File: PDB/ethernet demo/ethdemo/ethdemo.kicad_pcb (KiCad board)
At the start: 4 copper layers, 77.5 x 67.5 mm, 99 parts, among them J1 0826-1X1T-GJ-F, J2 0826-1X1T-GJ-F, J3 Conn_01x05_Socket, Q1 CSD19538Q3AT, U1 STM32H742VGTx, U2 KSZ8863RLLI, U3 TPS23861PWR, Y1 25MHz

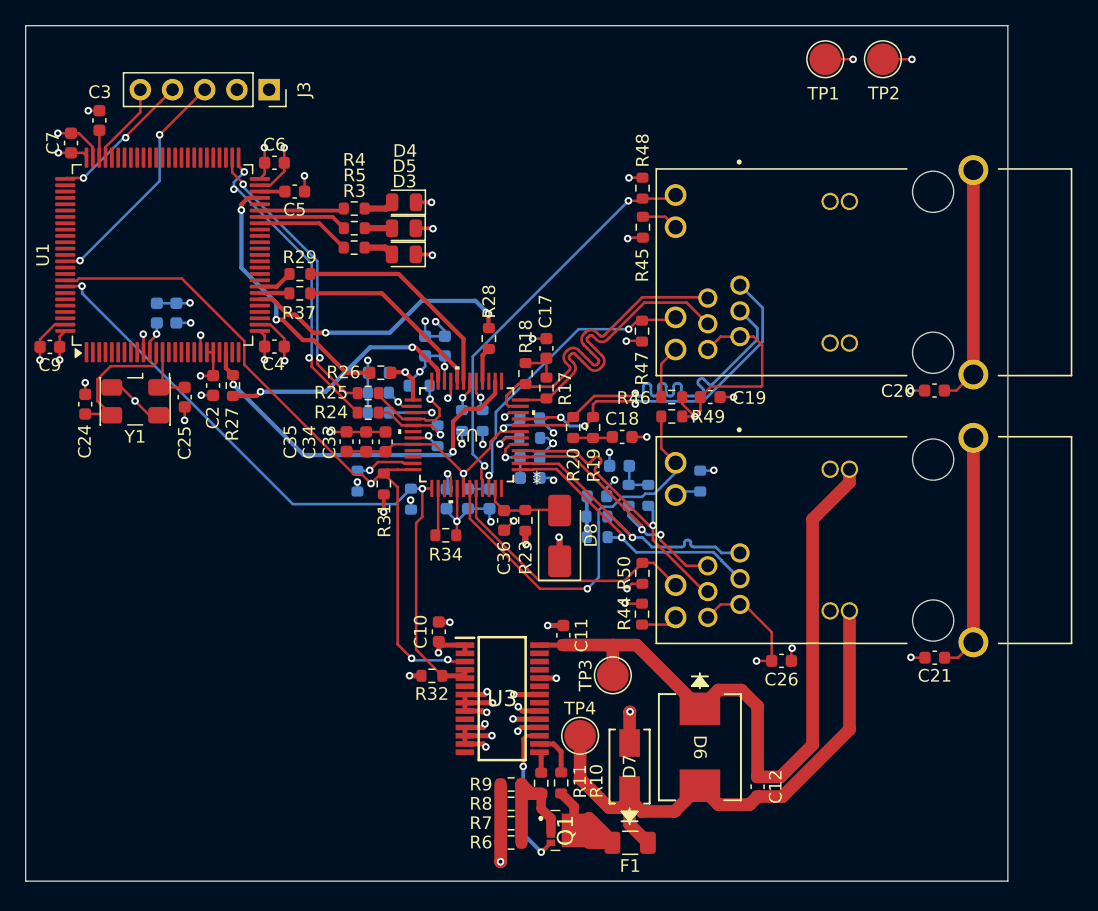
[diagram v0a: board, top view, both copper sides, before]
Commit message: routed usb and added power pads
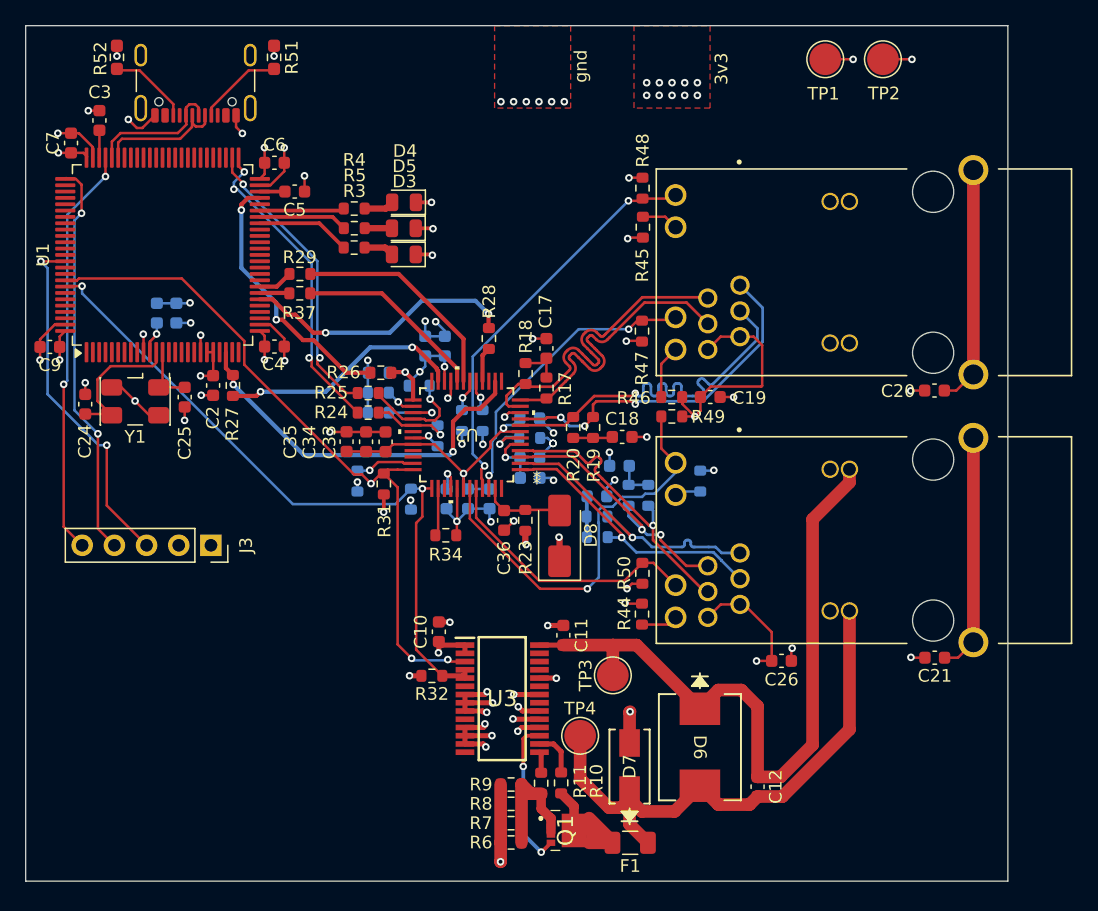
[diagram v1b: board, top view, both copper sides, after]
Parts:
- added J9: USB_C_Receptacle_USB2.0_16P, Connector_USB:USB_C_Receptacle_GCT_USB4105-xx-A_16P_TopMnt_Horizontal, F.Cu at (190.9, 40.9)
- added R51: 5.1k, Resistor_SMD:R_0603_1608Metric_Pad0.98x0.95mm_HandSolder, F.Cu at (197.1, 40.0)
- added R52: 5.1k, Resistor_SMD:R_0603_1608Metric_Pad0.98x0.95mm_HandSolder, F.Cu at (184.7, 40.0)
- moved J3 36.2 mm to (192.1, 78.5)
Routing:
- net /SWDIO: track 6.50 -> 32.6 mm, vias 0 -> 2
- net /SWCLK: track 11.4 -> 31.6 mm
- net /D-: track 0.00 -> 10.9 mm
- net /D+: track 0.00 -> 10.9 mm
- net /SWO/TRACE: track 18.7 -> 28.2 mm
- net Net-(J9-CC1): track 0.00 -> 6.82 mm
- net Net-(J9-CC2): track 0.00 -> 6.33 mm
- net GND: track 110.6 -> 116.7 mm, vias 55 -> 65
- net +3.3V: vias 28 -> 38
- added copper zone on F.Cu, net +3.3V
- added copper zone on F.Cu, net GND
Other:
- board text added: "3v3"
- board text added: "gnd"

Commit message: Satisfy DRC
I added poor for 48V and expanded GND for 2 power supply clips, ran DRC with JLC minimums and fixed problems
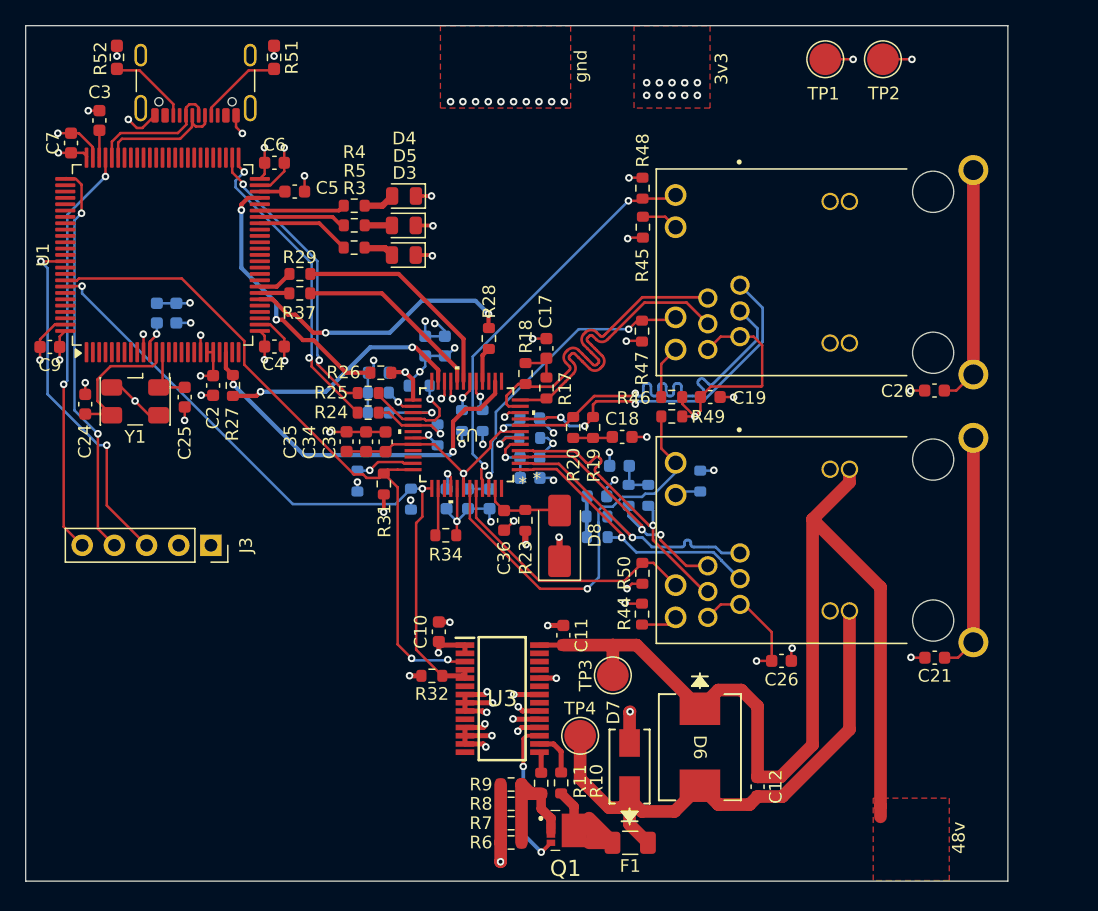
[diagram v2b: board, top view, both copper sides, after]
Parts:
- moved D4 0.50 mm to (207.4, 50.9)
- moved D5 0.23 mm to (207.3, 53.3)
- moved R4 0.23 mm to (203.4, 51.7)
- moved R5 0.22 mm to (203.4, 53.3)
- moved R42 0.07 mm to (210.0, 69.8)
- moved D3 0.05 mm to (207.3, 55.6)
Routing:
- net 48V: track 56.7 -> 82.4 mm
- net +3.3V: track 85.1 -> 85.9 mm, vias 38 -> 39
- net /TX-: track 25.0 -> 24.7 mm, vias 3 -> 2
- net /Clock: track 55.7 -> 55.6 mm, vias 3 -> 2
- net GND: vias 65 -> 68
- added copper zone on F.Cu, net 48V
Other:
- board text added: "48v"
